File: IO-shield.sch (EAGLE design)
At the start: 36 parts, among them J2 8x1F-H8.5, J3 8x1F-H8.5, J4 6x1F-H8.5

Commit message: extended shield with jumpers, added part list and picture
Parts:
- added J1: 10x1F-H8.5, SmartPrj:PINHD-1X10
- added JP10, JP11, JP12, JP13, JP14, JP15, JP16, JP2, JP3, JP4, JP5, JP6, JP7, JP8, JP9: (no value), jumper:JP1E
- JP1: value 10x1F-H8.5 -> (none); device SmartPrj:PINHD-1X10 -> jumper:JP1E
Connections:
- new net N$1: JP1.2, LED1.C
- new net N$17: JP15.1, R7.1, S7.S, S7.S1
- new net N$18: JP16.1, R8.1, S8.S, S8.S1
- new net N$19: JP3.2, LED3.C
- new net N$2: JP2.2, LED2.C
- new net N$20: JP4.2, LED4.C
- new net N$21: JP5.2, LED5.C
- new net N$22: JP6.2, LED6.C
- new net N$23: JP7.2, LED7.C
- new net N$24: JP8.2, LED8.C
- new net N$3: JP9.1, R1.1, S1.S, S1.S1
- new net N$4: JP10.1, R2.1, S2.S, S2.S1
- new net N$5: JP11.1, R3.1, S3.S, S3.S1
- new net N$6: JP12.1, R4.1, S4.S, S4.S1
- new net N$7: JP13.1, R5.1, S5.S, S5.S1
- new net N$8: JP14.1, R6.1, S6.S, S6.S1
- net GND: now also J1.7; no longer JP1.7
- net I1: now also J1.4, JP9.2; no longer JP1.4, R1.1, S1.S, S1.S1
- net I2: now also J1.3, JP10.2; no longer JP1.3, R2.1, S2.S, S2.S1
- net I3: now also J1.2, JP11.2; no longer JP1.2, R3.1, S3.S, S3.S1
- net I4: now also J1.1, JP12.2; no longer JP1.1, R4.1, S4.S, S4.S1
- net I5: now also JP13.2; no longer R5.1, S5.S, S5.S1
- net I6: now also JP14.2; no longer R6.1, S6.S, S6.S1
- net I7: now also JP15.2; no longer R7.1, S7.S, S7.S1
- net I8: now also JP16.2; no longer R8.1, S8.S, S8.S1
- net Q1: now also JP1.1; no longer LED1.C
- net Q2: now also JP2.1; no longer LED2.C
- net Q3: now also JP3.1; no longer LED3.C
- net Q4: now also JP4.1; no longer LED4.C
- net Q5: now also JP5.1; no longer LED5.C
- net Q6: now also JP6.1; no longer LED6.C
- net Q7: now also JP7.1; no longer LED7.C
- net Q8: now also JP8.1; no longer LED8.C

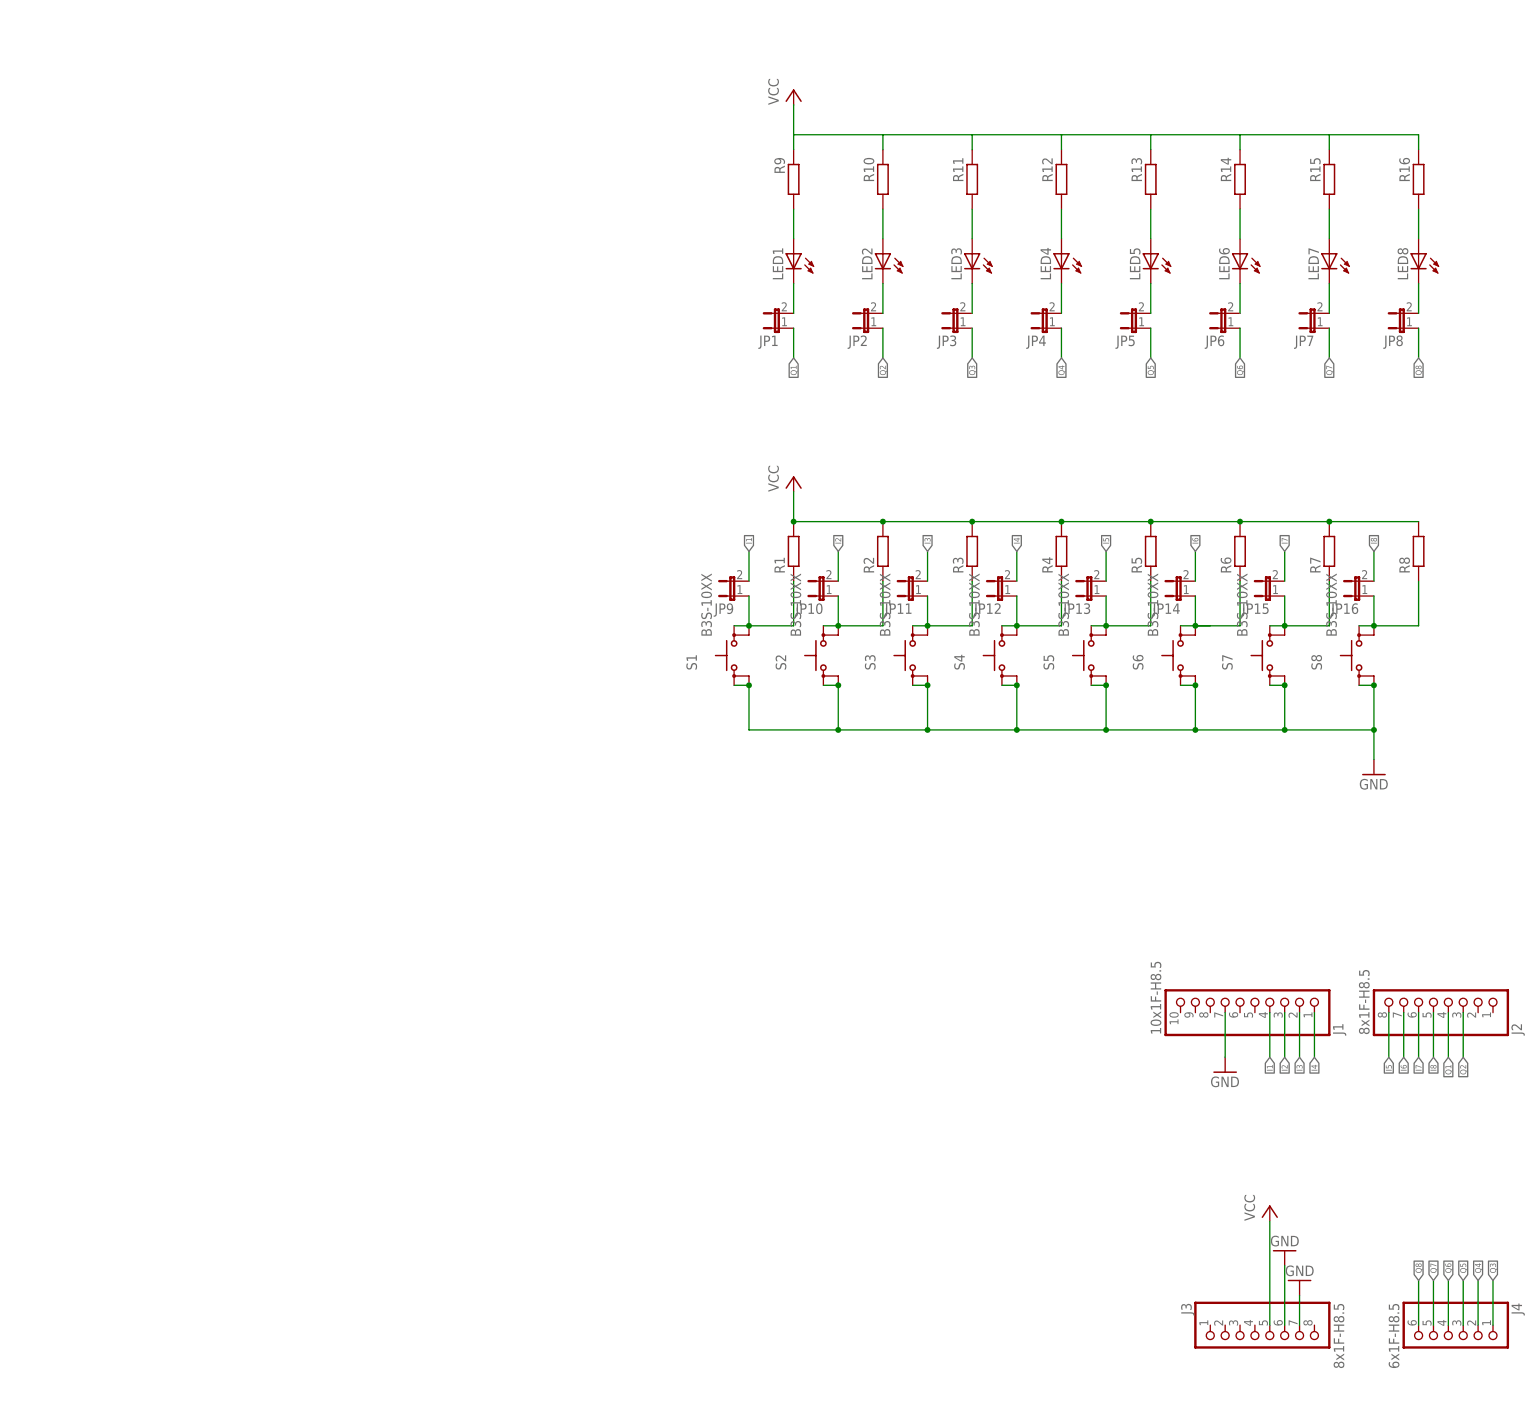
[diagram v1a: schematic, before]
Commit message: added 2 potis and header
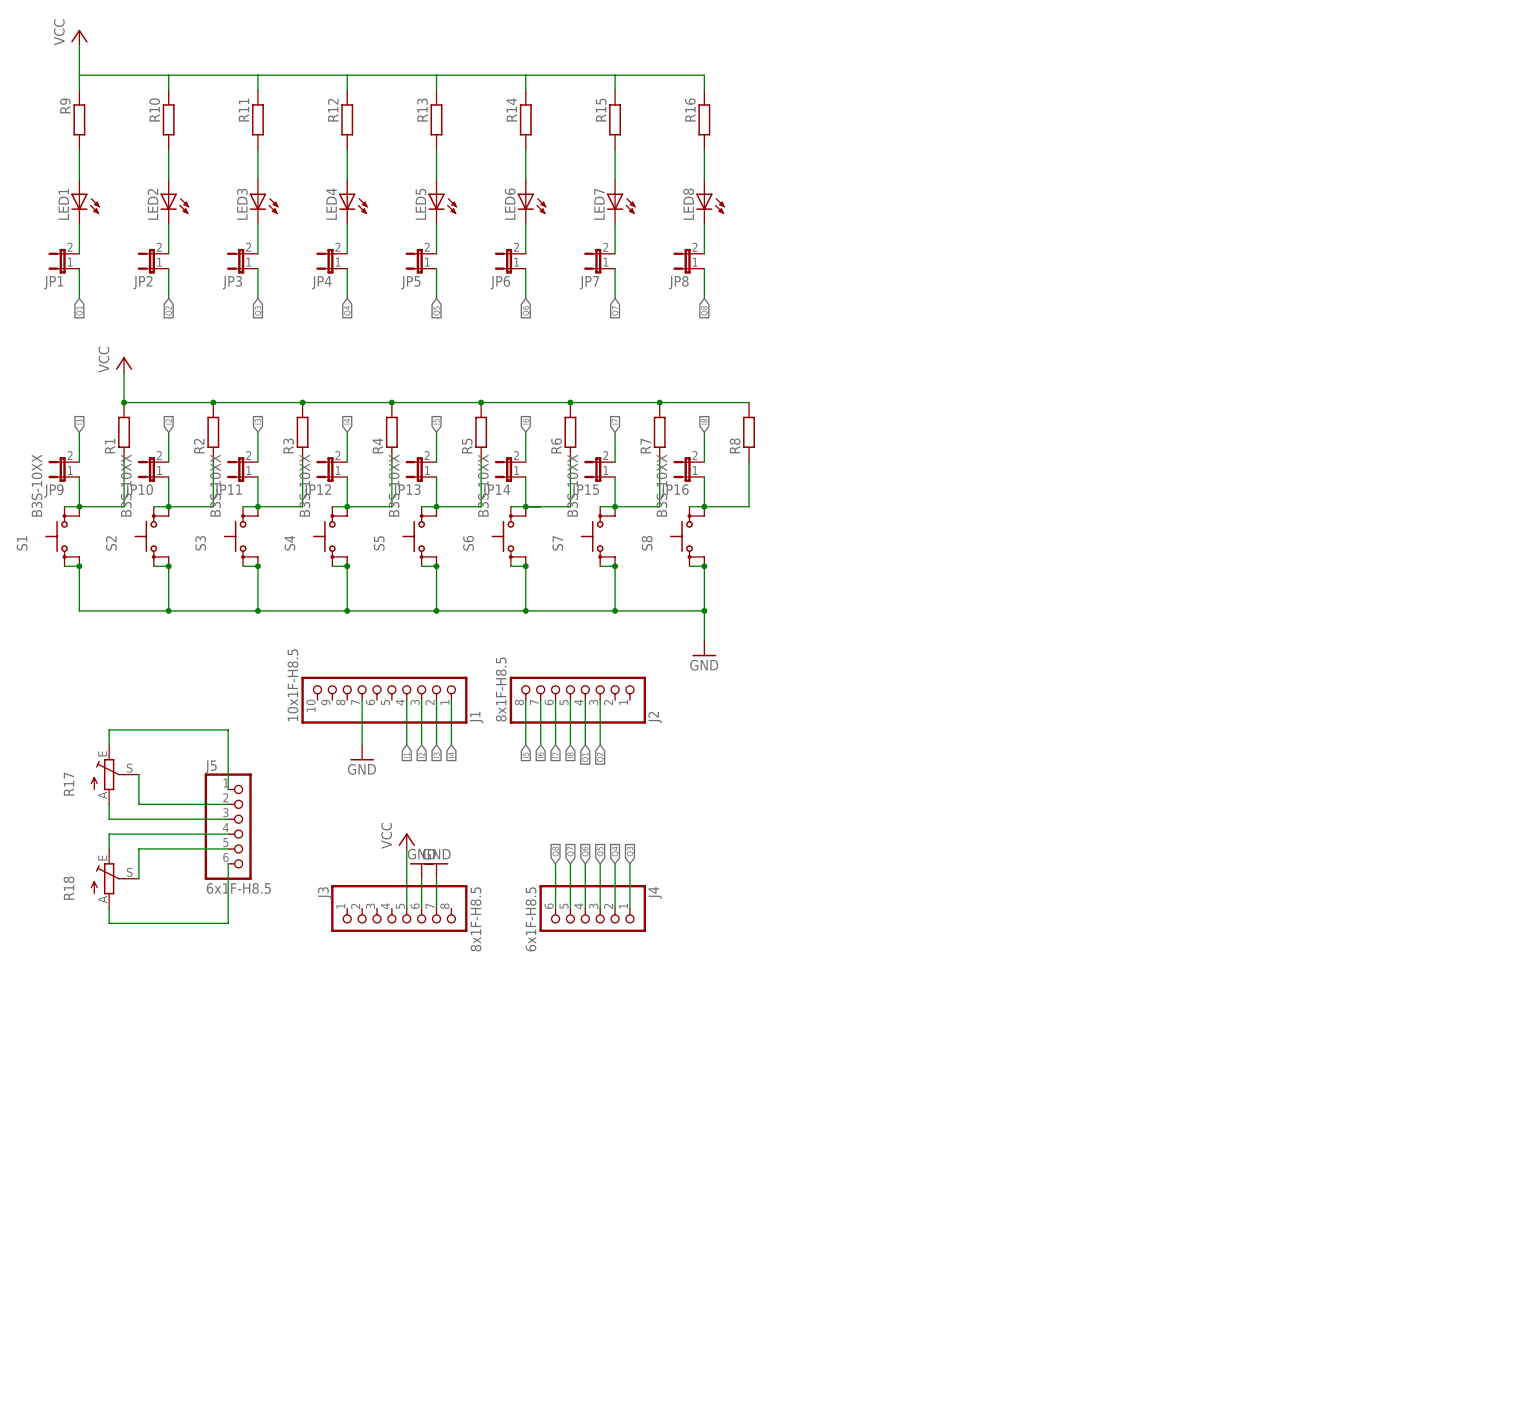
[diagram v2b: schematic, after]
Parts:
- added J5: 6x1F-H8.5, SmartPrj:PINHD-1X6
- added R17, R18: (no value), pot:TRIM_EU-CA6V
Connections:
- new net N$25: J5.2, R17.S
- new net N$26: J5.1, R17.E
- new net N$27: J5.3, R17.A
- new net N$28: J5.5, R18.S
- new net N$29: J5.4, R18.E
- new net N$30: J5.6, R18.A
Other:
- moved on the sheet: J1, J2, J3, J4, JP1, JP10, JP11, JP12, JP13, JP14, JP15, JP16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
